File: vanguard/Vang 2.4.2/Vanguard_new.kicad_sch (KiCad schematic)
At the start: 86 parts, among them J1 USB_C_Receptacle_USB2.0_16P, J2 Micro_SD_Card_Det1, J3 Conn_02x03_Odd_Even, J4 Conn_01x03, J5 Conn_01x03, J6 Conn_01x03, J7 Conn_01x02_Pin, Q1 BSS138, Q2 BSS138, Q3 BSS138, Q4 BSS138, U1 TXB0104D, U10 AP2112K-3.3, U2 TPS82130SILR, U3 ATSAMD11D14A-M, U4 BMP390L, U5 BD1020HFV-TR, U6 AT25DF641A-SH-T, U7 ATmega4809-A, U8 BNO055, U9 TPS61092, Y1 Crystal

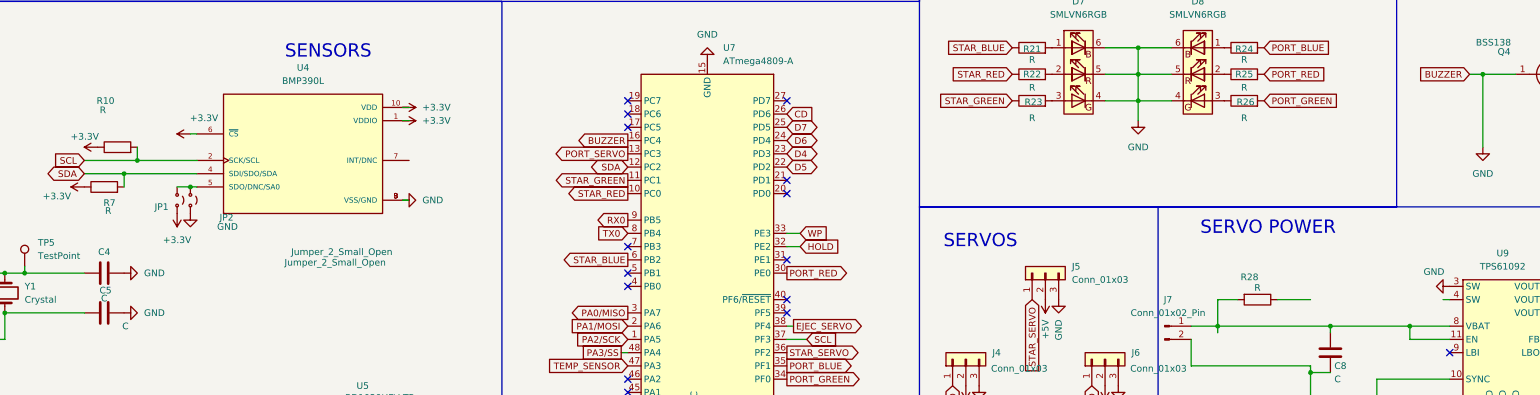
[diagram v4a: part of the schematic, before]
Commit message: changed inductor circuit
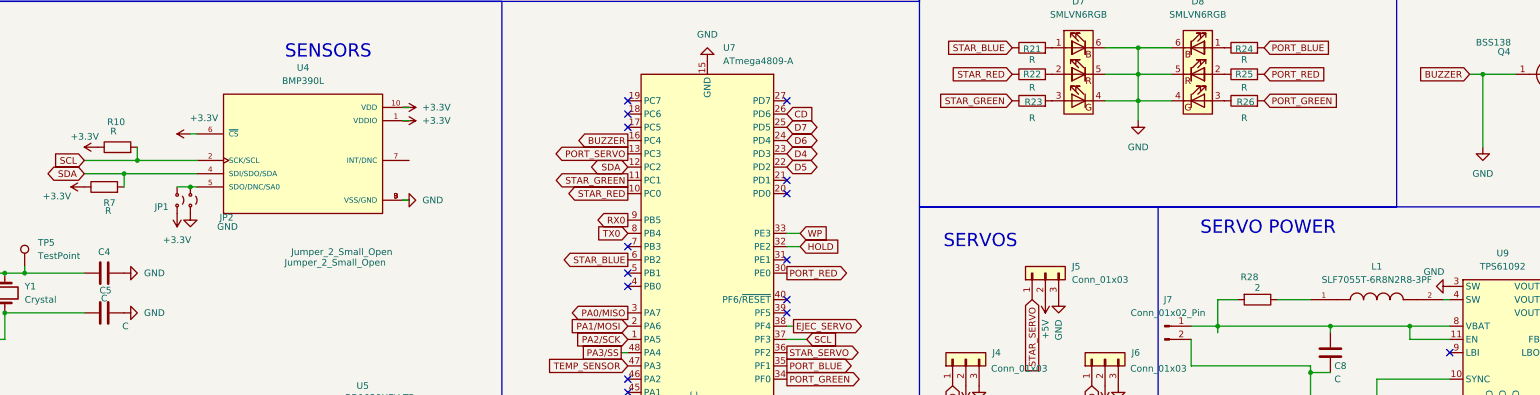
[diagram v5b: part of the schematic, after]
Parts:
- added L1: SLF7055T-6R8N2R8-3PF, SLF7055T-6R8N2R8-3PF:IND_SLF7055T-6R8N2R8-3PF, symbol SLF7055T-6R8N2R8-3PF[1]:SLF7055T-6R8N2R8-3PF
- R28: value R -> 2
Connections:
- net at U9.4 (SW): now also L1.2
- net at R28.1: now also L1.1
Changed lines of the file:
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@@
 		(dnp no)
 		(property "Reference" "R10"
-			(at 113.284 119.38 90)
+			(at 115.316 123.444 90)
 			(effects
 				(font
@@
 		)
 		(property "Value" "R"
-			(at 112.776 121.158 90)
+			(at 114.808 125.222 90)
 			(effects
 				(font
@@
 			)
 		)
-		(property "Value" "R"
+		(property "Value" "2"
 			(at 334.01 155.194 90)
 			(effects
@@
 					(unit 1)
 				)
+			)
+		)
+	)
+	(symbol
+		(lib_id "SLF7055T-6R8N2R8-3PF[1]:SLF7055T-6R8N2R8-3PF")
+		(at 356.87 157.48 0)
+		(unit 1)
+		(exclude_from_sim no)
+		(in_bom yes)
+		(on_board yes)
+		(dnp no)
+		(fields_autoplaced yes)
+		(property "Reference" "L1"
+			(at 356.87 151.13 0)
+			(effects
+				(font
+					(size 1.27 1.27)
+				)
+			)
+		)
+		(property "Value" "SLF7055T-6R8N2R8-3PF"
+			(at 356.87 153.67 0)
+			(effects
+				(font
+					(size 1.27 1.27)
+				)
+			)
+		)
+		(property "Footprint" "SLF7055T-6R8N2R8-3PF:IND_SLF7055T-6R8N2R8-3PF"
+			(at 356.87 157.48 0)
+			(effects
+				(font
+					(size 1.27 1.27)
+				)
+				(justify bottom)
+				(hide yes)
+			)
+		)
+		(property "Datasheet" ""
+			(at 356.87 157.48 0)
+			(effects
+				(font
+					(size 1.27 1.27)
+				)
+				(hide yes)
+			)
+		)
+		(property "Description" ""
+			(at 356.87 157.48 0)
+			(effects
+				(font
+					(size 1.27 1.27)
+				)
+				(hide yes)
+			)
+		)
+		(property "MF" "TDK"
+			(at 356.87 157.48 0)
+			(effects
+				(font
+					(size 1.27 1.27)
+				)
+				(justify bottom)
+				(hide yes)
+			)
+		)
+		(property "MAXIMUM_PACKAGE_HEIGHT" "5.8 mm"
+			(at 356.87 157.48 0)
+			(effects
+				(font
+					(size 1.27 1.27)
+				)
+				(justify bottom)
+				(hide yes)
+			)
+		)
+		(property "Package" "NON STANDARD-2 TDK"
+			(at 356.87 157.48 0)
+			(effects
+				(font
+					(size 1.27 1.27)
+				)
+				(justify bottom)
+				(hide yes)
+			)
+		)
+		(property "Price" "None"
+			(at 356.87 157.48 0)
+			(effects
+				(font
+					(size 1.27 1.27)
+				)
+				(justify bottom)
+				(hide yes)
+			)
+		)
+		(property "Check_prices" "https://www.snapeda.com/parts/SLF7055T-6R8N2R8-3PF/TDK/view-part/?ref=eda"
+			(at 356.87 157.48 0)
+			(effects
+				(font
+					(size 1.27 1.27)
+				)
+				(justify bottom)
+				(hide yes)
+			)
+		)
+		(property "STANDARD" "Manufacturer Recommendations"
+			(at 356.87 157.48 0)
+			(effects
+				(font
+					(size 1.27 1.27)
+				)
+				(justify bottom)
+				(hide yes)
+			)
+		)
+		(property "PARTREV" "N/A"
+			(at 356.87 157.48 0)
+			(effects
+				(font
+					(size 1.27 1.27)
+				)
+				(justify bottom)
+				(hide yes)
+			)
+		)
+		(property "SnapEDA_Link" "https://www.snapeda.com/parts/SLF7055T-6R8N2R8-3PF/TDK/view-part/?ref=snap"
+			(at 356.87 157.48 0)
+			(effects
+				(font
+					(size 1.27 1.27)
+				)
+				(justify bottom)
+				(hide yes)
+			)
+		)
+		(property "MP" "SLF7055T-6R8N2R8-3PF"
+			(at 356.87 157.48 0)
+			(effects
+				(font
+					(size 1.27 1.27)
+				)
+				(justify bottom)
+				(hide yes)
+			)
+		)
+		(property "Description_1" "Inductor Power Shielded Wirewound 6.8uH 30% 100KHz Ferrite 2.8A 44.2mOhm DCR T/R"
+			(at 356.87 157.48 0)
+			(effects
+				(font
+					(size 1.27 1.27)
+				)
+				(justify bottom)
+				(hide yes)
+			)
+		)
+		(property "Availability" "In Stock"
+			(at 356.87 157.48 0)
+			(effects
+				(font
+					(size 1.27 1.27)
+				)
+				(justify bottom)
+				(hide yes)
+			)
+		)
+		(property "MANUFACTURER" "TDK"
+			(at 356.87 157.48 0)
+			(effects
+				(font
+					(size 1.27 1.27)
+				)
+				(justify bottom)
+				(hide yes)
+			)
+		)
+		(pin "2"
+		)
+		(pin "1"
+		)
+		(instances
+			(project ""
+				(path "/972fbf12-2dcd-4fdf-b1c9-8a2880c46640"
+					(reference "L1")
+					(unit 1)
+				)

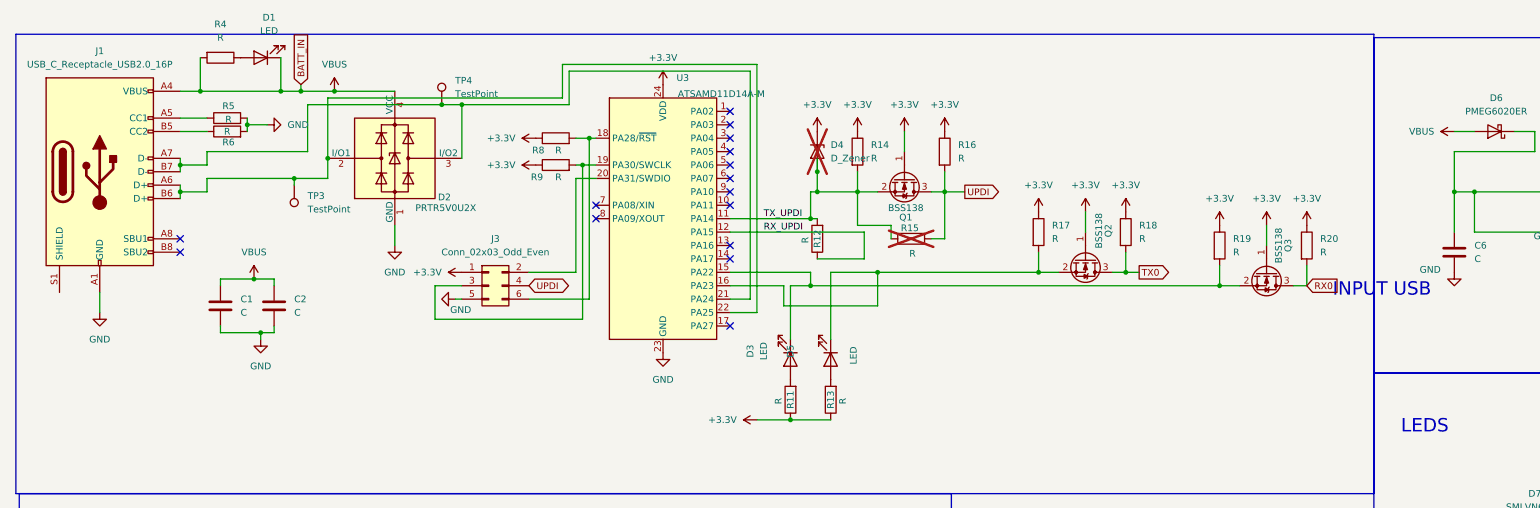
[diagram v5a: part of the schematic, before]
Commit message: Input USB - r and c assign
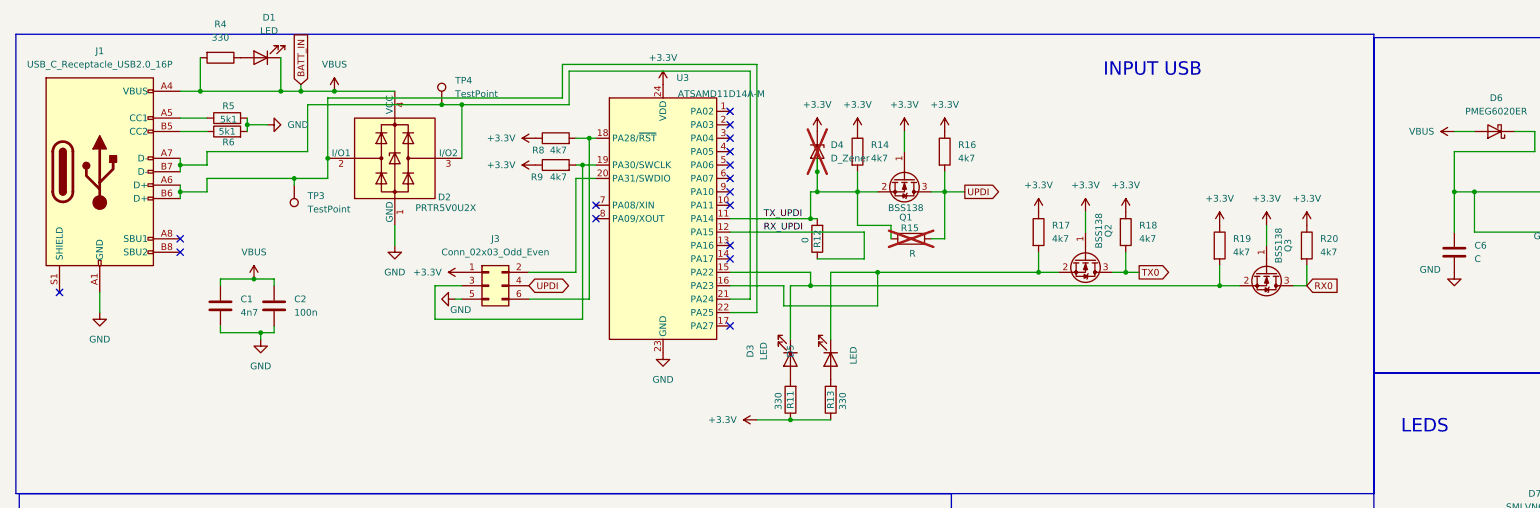
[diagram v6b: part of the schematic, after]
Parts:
- C1: value C -> 4n7
- C2: value C -> 100n
- R11, R13, R4: value R -> 330
- R12: value R -> 0
- R14, R16, R17, R18, R19, R20, R8, R9: value R -> 4k7
- R5, R6: value R -> 5k1
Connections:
- no-connect marks 42 -> 43
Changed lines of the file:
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@@
 	(text "INPUT USB"
 		(exclude_from_sim no)
-		(at 270.764 61.722 0)
+		(at 227.33 20.066 0)
 		(effects
 			(font
@@
 	)
 	(no_connect
+		(at 20.32 62.23)
+	)
+	(no_connect
 		(at 147.32 33.02)
 	)
@@
 			)
 		)
-		(property "Value" "R"
+		(property "Value" "4k7"
 			(at 208.28 52.0699 0)
 			(effects
@@
 			)
 		)
-		(property "Value" "R"
+		(property "Value" "4k7"
 			(at 114.808 35.306 90)
 			(effects
@@
 			)
 		)
-		(property "Value" "R"
+		(property "Value" "4k7"
 			(at 259.08 54.6099 0)
 			(effects
@@
 			)
 		)
-		(property "Value" "R"
+		(property "Value" "4k7"
 			(at 190.5 36.8299 0)
 			(effects
@@
 			)
 		)
-		(property "Value" "C"
+		(property "Value" "100n"
 			(at 64.77 66.0399 0)
 			(effects
@@
 			)
 		)
-		(property "Value" "R"
+		(property "Value" "330"
 			(at 50.8 13.97 90)
 			(effects
@@
 			)
 		)
-		(property "Value" "R"
+		(property "Value" "5k1"
 			(at 52.324 29.464 90)
 			(effects
@@
 			)
 		)
-		(property "Value" "R"
+		(property "Value" "4k7"
 			(at 114.808 40.386 90)
 			(effects
@@
 			)
 		)
-		(property "Value" "R"
+		(property "Value" "4k7"
 			(at 242.57 54.6099 0)
 			(effects
@@
 			)
 		)
-		(property "Value" "R"
+		(property "Value" "4k7"
 			(at 224.79 52.0699 0)
 			(effects
@@
 			)
 		)
-		(property "Value" "R"
+		(property "Value" "330"
 			(at 168.656 82.804 90)
 			(effects
@@
 			)
 		)
-		(property "Value" "R"
+		(property "Value" "330"
 			(at 156.464 82.804 90)
 			(effects
@@
 			)
 		)
-		(property "Value" "R"
+		(property "Value" "0"
 			(at 161.544 52.324 90)
 			(effects
@@
 			)
 		)
-		(property "Value" "R"
+		(property "Value" "4k7"
 			(at 173.99 36.8299 0)
 			(effects
@@
 			)
 		)
-		(property "Value" "C"
+		(property "Value" "4n7"
 			(at 54.61 66.0399 0)
 			(effects
@@
 			)
 		)
-		(property "Value" "R"
+		(property "Value" "5k1"
 			(at 52.07 31.75 90)
 			(effects

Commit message: power stabilization
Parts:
- C10: value C -> 22u
- C11, C9: value C -> 1u
- C6: value C -> 10u
- C7: value C -> 3n3
- R27, R30: value R -> 100k
- R29: value R -> 124k
- R31, R33: value R -> 330
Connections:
- net GND: now also D1.1 (K)
- net VBUS: no longer D1.1 (K)
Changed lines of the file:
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@@
 	)
 	(junction
-		(at 62.23 24.13)
-		(diameter 0)
-		(color 0 0 0 0)
-	)
-	(junction
 		(at 393.7 154.94)
 		(diameter 0)
@@
 	(wire
 		(pts
+			(xy 307.34 40.64) (xy 307.34 41.91)
+		)
+		(stroke
+			(width 0)
+			(type default)
+		)
+	)
+	(wire
+		(pts
 			(xy 66.04 24.13) (xy 72.39 24.13)
 		)
@@
 	(wire
 		(pts
-			(xy 393.7 39.37) (xy 398.78 39.37)
+			(xy 62.23 17.78) (xy 77.47 17.78)
 		)
 		(stroke
@@
 	(wire
 		(pts
-			(xy 304.8 114.3) (xy 311.15 114.3)
+			(xy 393.7 39.37) (xy 398.78 39.37)
 		)
 		(stroke
@@
 	(wire
 		(pts
-			(xy 97.79 151.13) (xy 97.79 152.4)
+			(xy 304.8 114.3) (xy 311.15 114.3)
 		)
 		(stroke
@@
 	(wire
 		(pts
-			(xy 306.07 40.64) (xy 306.07 41.91)
+			(xy 97.79 151.13) (xy 97.79 152.4)
 		)
 		(stroke
@@
 	(wire
 		(pts
-			(xy 62.23 24.13) (xy 66.04 24.13)
+			(xy 46.99 24.13) (xy 66.04 24.13)
 		)
 		(stroke
@@
 	(wire
 		(pts
-			(xy 308.61 40.64) (xy 306.07 40.64)
+			(xy 308.61 40.64) (xy 307.34 40.64)
 		)
 		(stroke
@@
 	(wire
 		(pts
-			(xy 344.17 50.8) (xy 344.17 52.07)
-		)
-		(stroke
-			(width 0)
-			(type default)
-		)
-	)
-	(wire
-		(pts
 			(xy 361.95 64.77) (xy 361.95 66.04)
 		)
@@
 	(wire
 		(pts
+			(xy 344.17 50.8) (xy 344.17 52.07)
+		)
+		(stroke
+			(width 0)
+			(type default)
+		)
+	)
+	(wire
+		(pts
 			(xy 240.03 57.15) (xy 240.03 60.96)
 		)
@@
 	(wire
 		(pts
+			(xy 307.34 41.91) (xy 306.07 41.91)
+		)
+		(stroke
+			(width 0)
+			(type default)
+		)
+	)
+	(wire
+		(pts
 			(xy 43.18 29.21) (xy 48.26 29.21)
 		)
@@
 	(wire
 		(pts
-			(xy 62.23 17.78) (xy 62.23 24.13)
-		)
-		(stroke
-			(width 0)
-			(type default)
-		)
-	)
-	(wire
-		(pts
-			(xy 46.99 24.13) (xy 62.23 24.13)
-		)
-		(stroke
-			(width 0)
-			(type default)
-		)
-	)
-	(wire
-		(pts
 			(xy 46.99 17.78) (xy 46.99 24.13)
 		)
@@
 	(wire
 		(pts
-			(xy 288.29 50.8) (xy 288.29 43.18)
+			(xy 288.29 43.18) (xy 288.29 50.8)
 		)
 		(stroke
@@
 			)
 		)
-		(property "Value" "C"
+		(property "Value" "1u"
 			(at 369.57 44.4499 0)
 			(effects
@@
 			)
 		)
-		(property "Value" "R"
+		(property "Value" "100k"
 			(at 350.52 31.75 90)
 			(effects
@@
 			)
 		)
-		(property "Value" "R"
+		(property "Value" "330"
 			(at 412.75 44.4499 0)
 			(effects
@@
 			)
 		)
-		(property "Value" "R"
+		(property "Value" "124k"
 			(at 355.6 43.1799 0)
 			(effects
@@
 			)
 		)
-		(property "Value" "C"
+		(property "Value" "1u"
 			(at 402.59 44.4499 0)
 			(effects
@@
 			)
 		)
-		(property "Value" "C"
+		(property "Value" "3n3"
 			(at 309.88 46.9899 0)
 			(effects
@@
 	)
 	(symbol
+		(lib_id "power:GND")
+		(at 77.47 17.78 90)
+		(unit 1)
+		(exclude_from_sim no)
+		(in_bom yes)
+		(on_board yes)
+		(dnp no)
+		(fields_autoplaced yes)
+		(property "Reference" "#PWR0182"
+			(at 83.82 17.78 0)
+			(effects
+				(font
+					(size 1.27 1.27)
+				)
+				(hide yes)
+			)
+		)
+		(property "Value" "GND"
+			(at 81.28 17.7799 90)
+			(effects
+				(font
+					(size 1.27 1.27)
+				)
+				(justify right)
+			)
+		)
+		(property "Footprint" ""
+			(at 77.47 17.78 0)
+			(effects
+				(font
+					(size 1.27 1.27)
+				)
+				(hide yes)
+			)
+		)
+		(property "Datasheet" ""
+			(at 77.47 17.78 0)
+			(effects
+				(font
+					(size 1.27 1.27)
+				)
+				(hide yes)
+			)
+		)
+		(property "Description" "Power symbol creates a global label with name \"GND\" , ground"
+			(at 77.47 17.78 0)
+			(effects
+				(font
+					(size 1.27 1.27)
+				)
+				(hide yes)
+			)
+		)
+		(pin "1"
+		)
+		(instances
+			(project "Vanguard_new"
+				(path "/972fbf12-2dcd-4fdf-b1c9-8a2880c46640"
+					(reference "#PWR0182")
+					(unit 1)
+				)
+			)
+		)
+	)
+	(symbol
 		(lib_id "Device:R")
 		(at 33.02 162.56 0)
@@
 			)
 		)
-		(property "Value" "R"
+		(property "Value" "100k"
 			(at 355.6 55.8799 0)
 			(effects
@@
 			)
 		)
-		(property "Value" "C"
+		(property "Value" "22u"
 			(at 377.19 44.4499 0)
 			(effects
@@
 			)
 		)
-		(property "Value" "R"
+		(property "Value" "330"
 			(at 364.49 62.2299 0)
 			(effects
@@
 			)
 		)
-		(property "Value" "C"
+		(property "Value" "10u"
 			(at 288.29 55.8799 0)
 			(effects

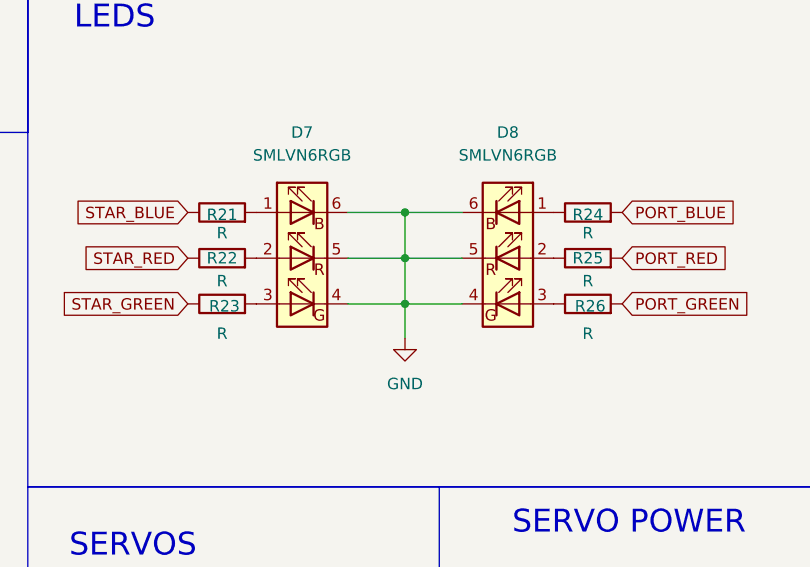
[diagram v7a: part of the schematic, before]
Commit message: leds starboard
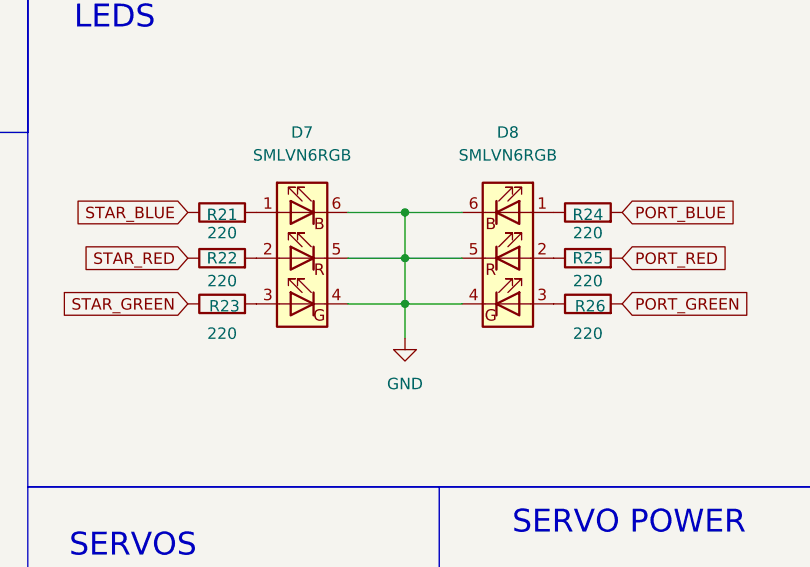
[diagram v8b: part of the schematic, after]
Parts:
- R21, R22, R23, R24, R25, R26: value R -> 220
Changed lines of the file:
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@@
 			)
 		)
-		(property "Value" "R"
+		(property "Value" "220"
 			(at 290.83 111.506 90)
 			(effects
@@
 			)
 		)
-		(property "Value" "R"
+		(property "Value" "220"
 			(at 331.47 122.682 90)
 			(effects
@@
 			)
 		)
-		(property "Value" "R"
+		(property "Value" "220"
 			(at 290.83 122.682 90)
 			(effects
@@
 			)
 		)
-		(property "Value" "R"
+		(property "Value" "220"
 			(at 290.83 116.84 90)
 			(effects
@@
 			)
 		)
-		(property "Value" "R"
+		(property "Value" "220"
 			(at 331.47 116.84 90)
 			(effects
@@
 			)
 		)
-		(property "Value" "R"
+		(property "Value" "220"
 			(at 331.47 111.506 90)
 			(effects
